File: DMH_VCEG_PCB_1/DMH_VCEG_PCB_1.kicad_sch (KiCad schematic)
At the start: 0 parts

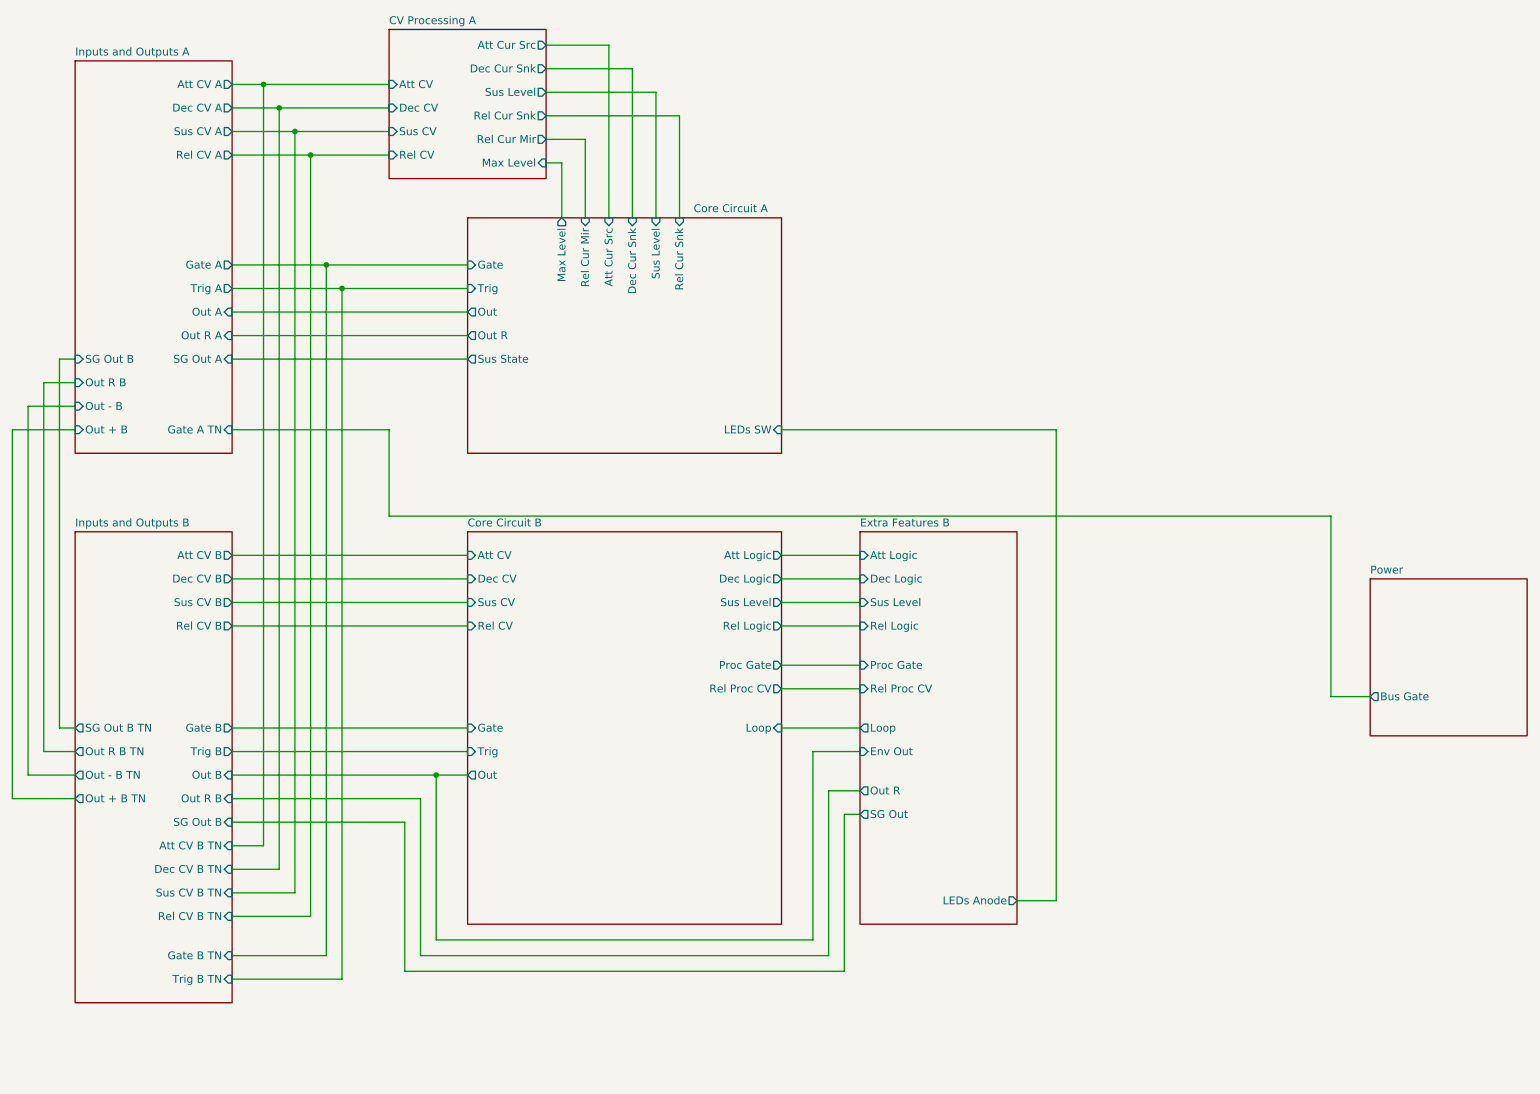
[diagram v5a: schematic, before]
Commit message: Copied circuit A to B
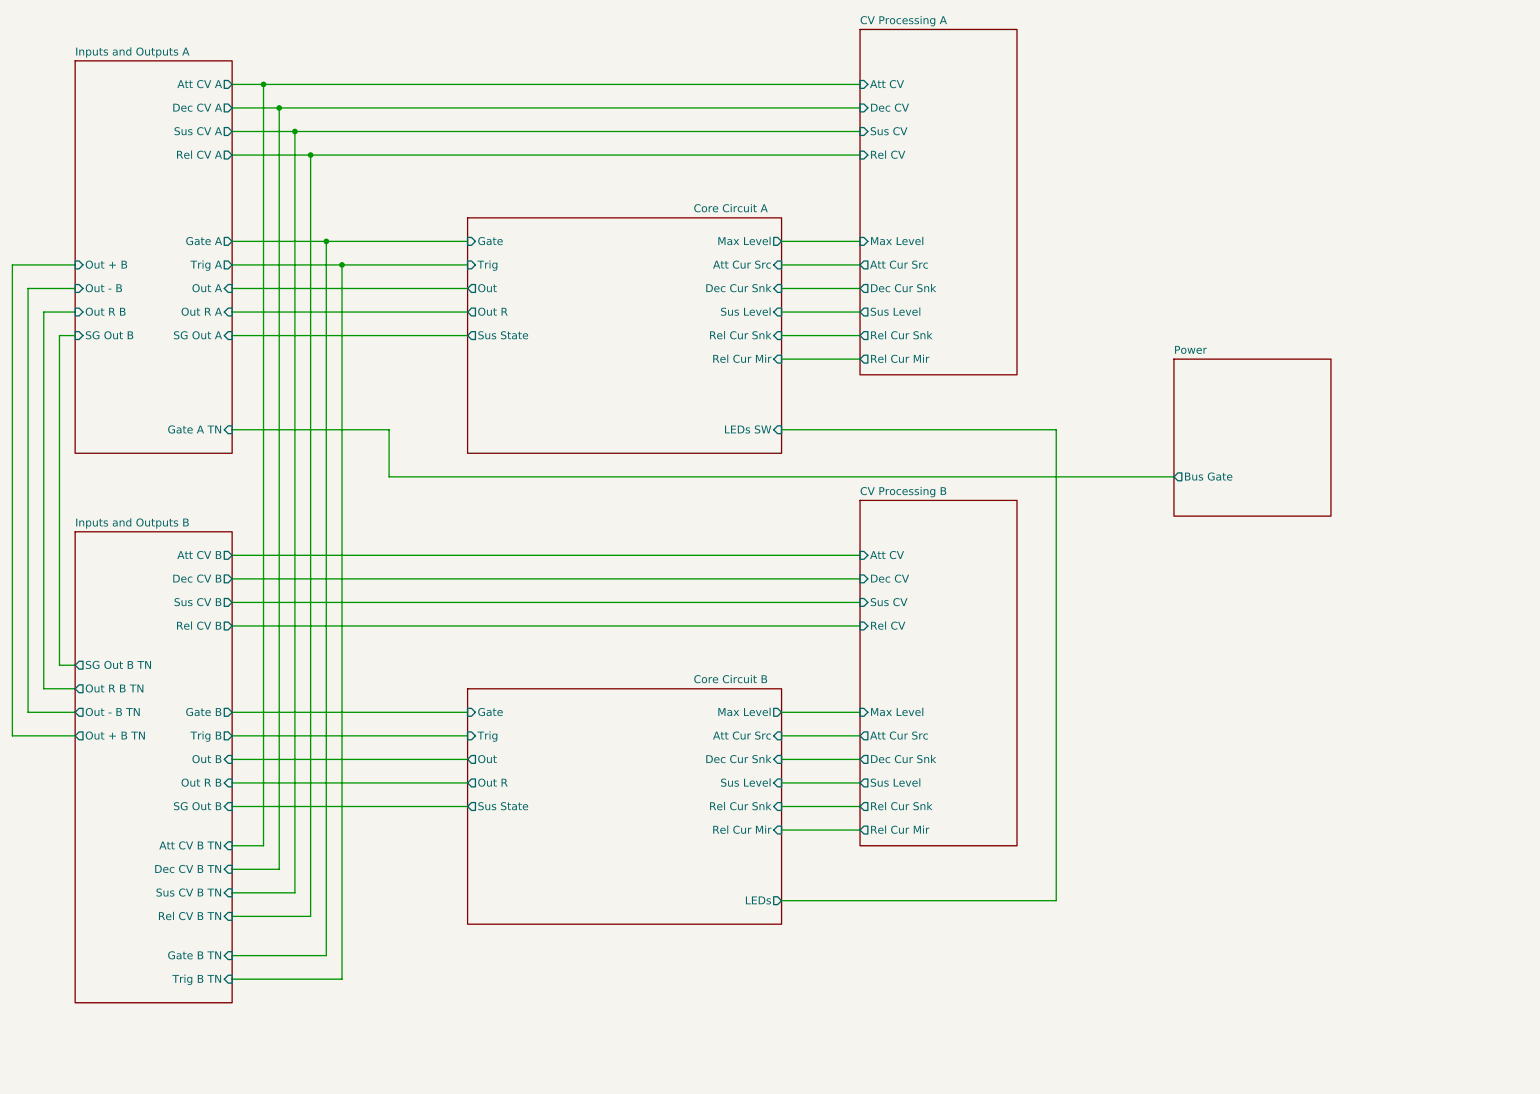
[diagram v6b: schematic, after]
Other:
- removed sheet Extra Features B
- added sheet CV Processing B (CV_Processing_B.kicad_sch)
- sheet Core Circuit B ports: added Att Cur Src, Dec Cur Snk, LEDs, Max Level, Out R, Rel Cur Mir, Rel Cur Snk, Sus State; removed Att CV, Att Logic, Dec CV, Dec Logic, Loop, Proc Gate, Rel CV, Rel Logic, Rel Proc CV, Sus CV

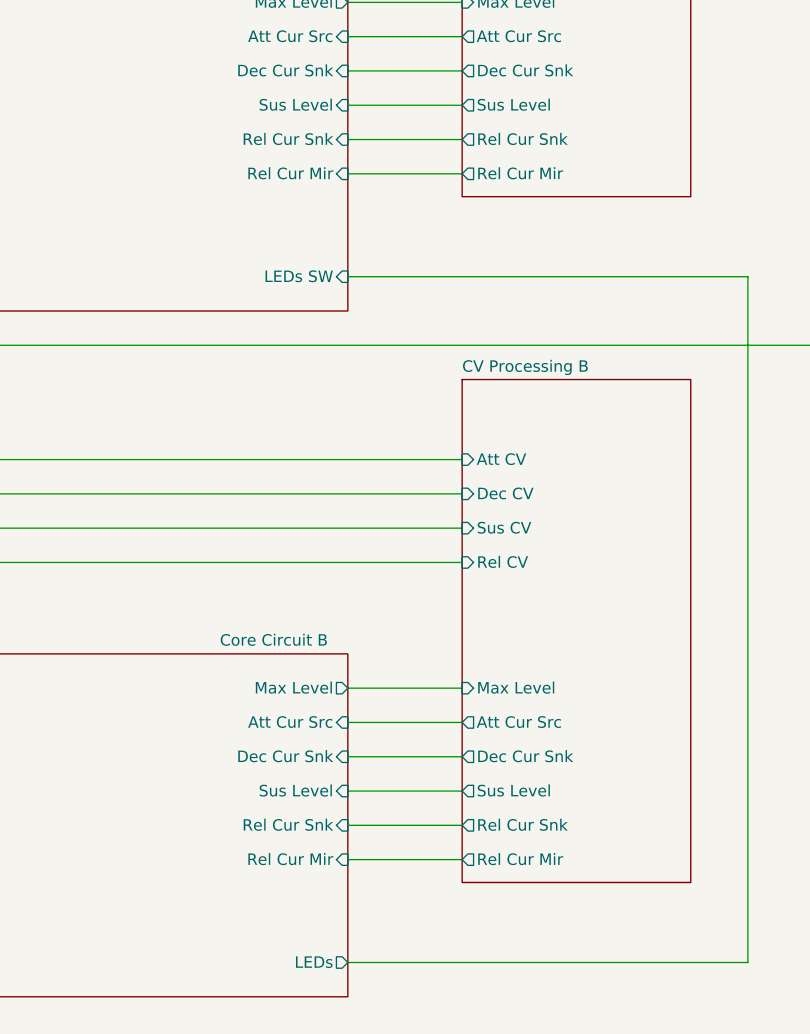
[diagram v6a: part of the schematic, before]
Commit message: Copied Circuit A into B
And added diode to protect input of U3B
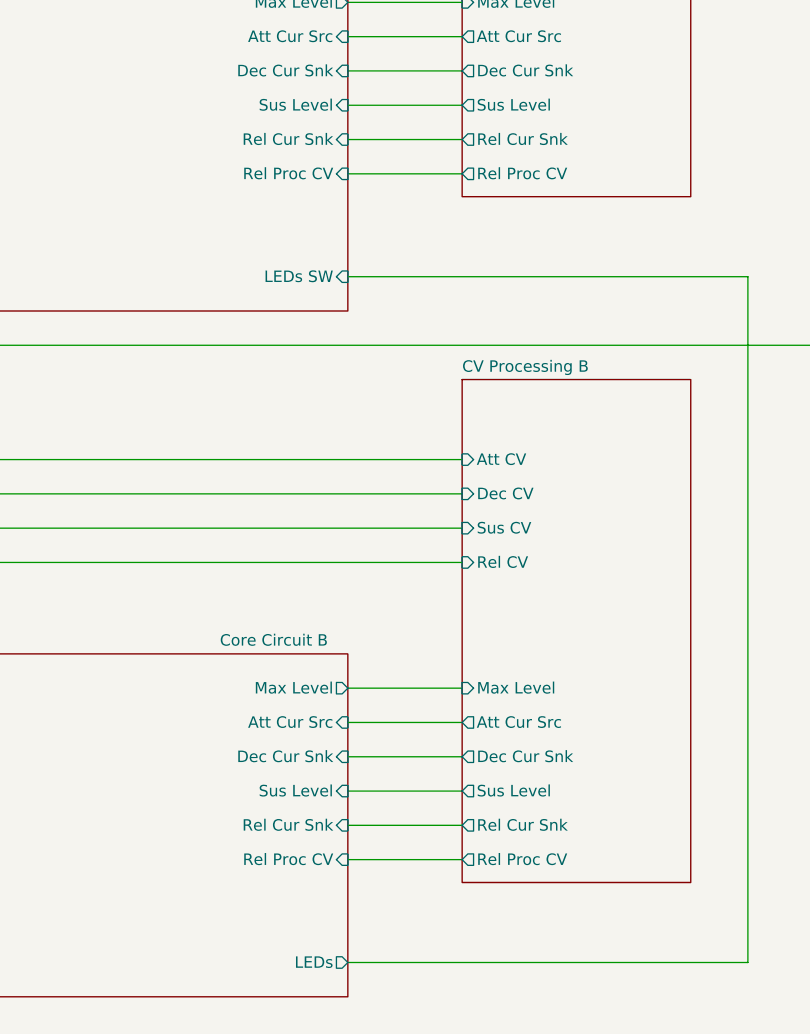
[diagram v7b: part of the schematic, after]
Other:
- sheet CV Processing A ports: added Rel Proc CV; removed Rel Cur Mir
- sheet CV Processing B ports: added Rel Proc CV; removed Rel Cur Mir
- sheet Core Circuit A ports: added Rel Proc CV; removed Rel Cur Mir
- sheet Core Circuit B ports: added Rel Proc CV; removed Rel Cur Mir
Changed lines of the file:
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@@
 			)
 		)
-		(pin "Rel Cur Mir" output
+		(pin "Rel Proc CV" output
 			(at 165.1 73.66 180)
 			(effects
@@
 			)
 		)
-		(pin "Rel Cur Mir" input
+		(pin "Rel Proc CV" input
 			(at 152.4 149.86 0)
 			(effects
@@
 			)
 		)
-		(pin "Rel Cur Mir" output
+		(pin "Rel Proc CV" output
 			(at 165.1 149.86 180)
 			(effects
@@
 			)
 		)
-		(pin "Rel Cur Mir" input
+		(pin "Rel Proc CV" input
 			(at 152.4 73.66 0)
 			(effects

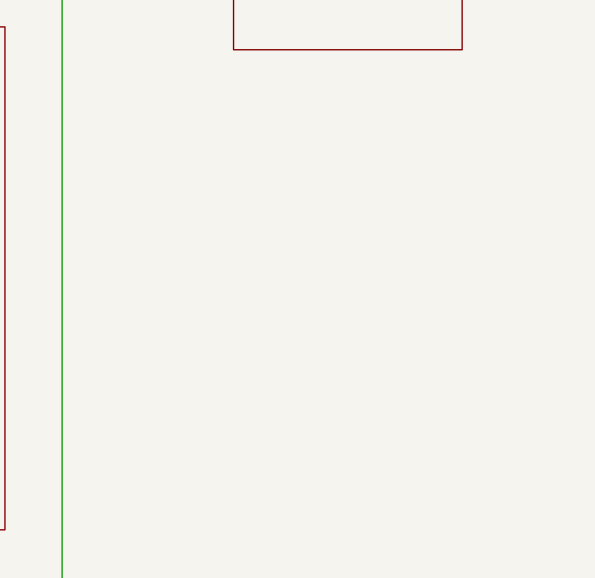
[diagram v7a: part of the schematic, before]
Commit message: Added breadboard layout drawing
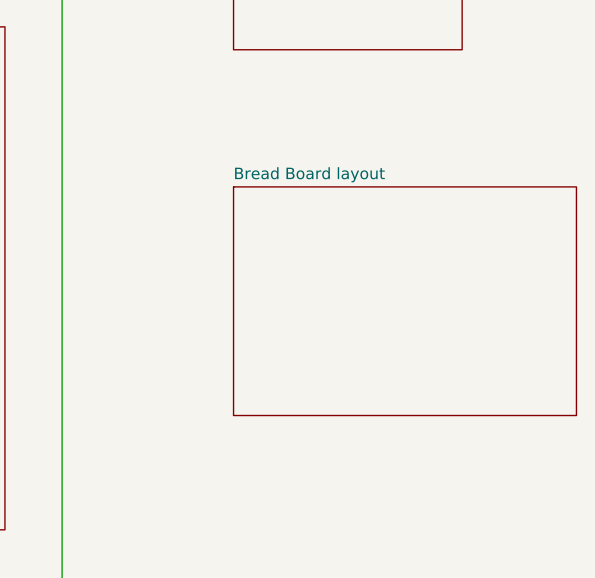
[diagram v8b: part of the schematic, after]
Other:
- added sheet Bread Board layout (bb_layout.kicad_sch)
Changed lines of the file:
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@@
+	)
+	(sheet
+		(at 215.9 114.3)
+		(size 38.1 25.4)
+		(exclude_from_sim no)
+		(in_bom yes)
+		(on_board yes)
+		(dnp no)
+		(fields_autoplaced yes)
+		(stroke
+			(width 0.1524)
+			(type solid)
+		)
+		(fill
+			(color 0 0 0 0.0000)
+		)
+		(property "Sheetname" "Bread Board layout"
+			(at 215.9 113.5884 0)
+			(effects
+				(font
+					(size 1.27 1.27)
+				)
+				(justify left bottom)
+			)
+		)
+		(property "Sheetfile" "bb_layout.kicad_sch"
+			(at 215.9 140.2846 0)
+			(effects
+				(font
+					(size 1.27 1.27)
+				)
+				(justify left top)
+				(hide yes)
+			)
+		)
+		(instances
+			(project "DMH_VCEG_PCB_1"
+				(path "/58f4306d-5387-4983-bb08-41a2313fd315"
+					(page "9")
+				)
+			)
+		)
 	)
 	(sheet
